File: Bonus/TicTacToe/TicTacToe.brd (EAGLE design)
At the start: 78.4 x 78.4 mm, 61 parts

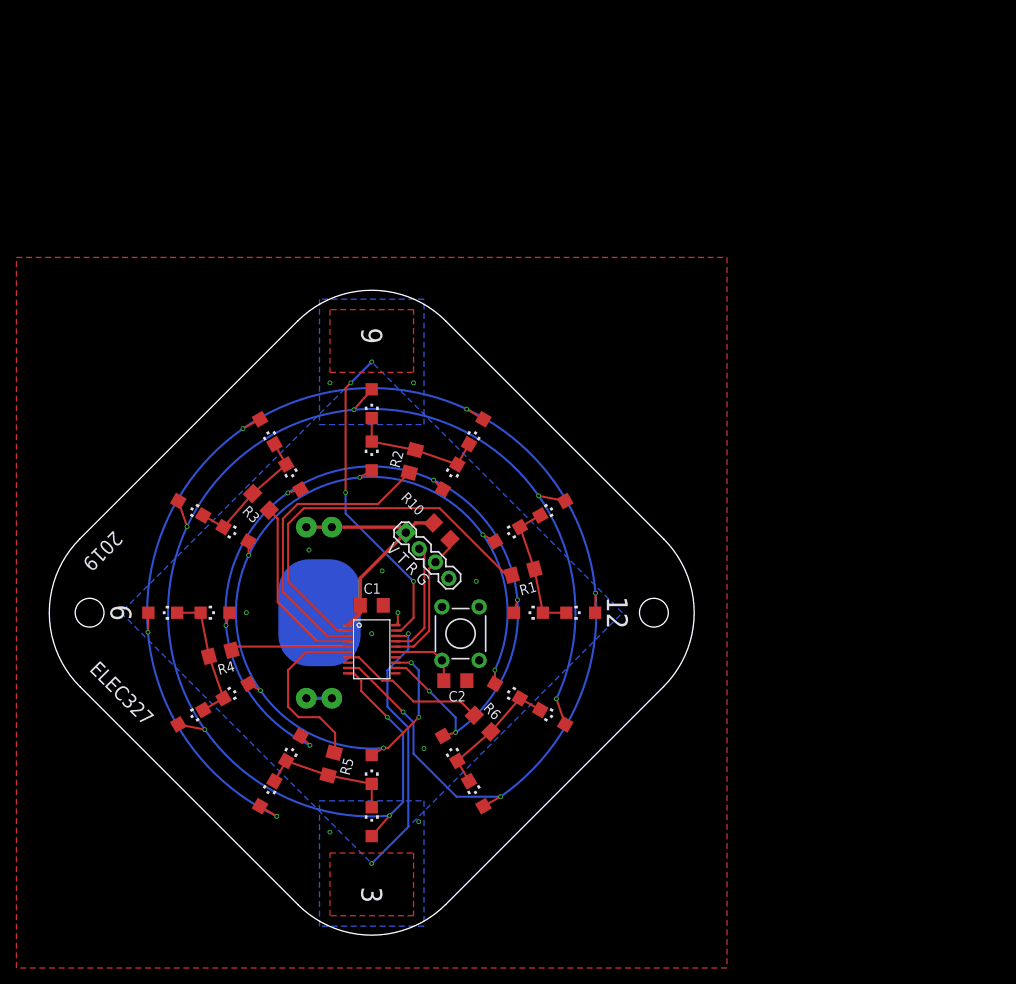
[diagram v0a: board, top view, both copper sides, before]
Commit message: Restored original 2020 pendant in directory, made a new directory for 2021 fabbed pendant, and a directory for Bonus PCB.
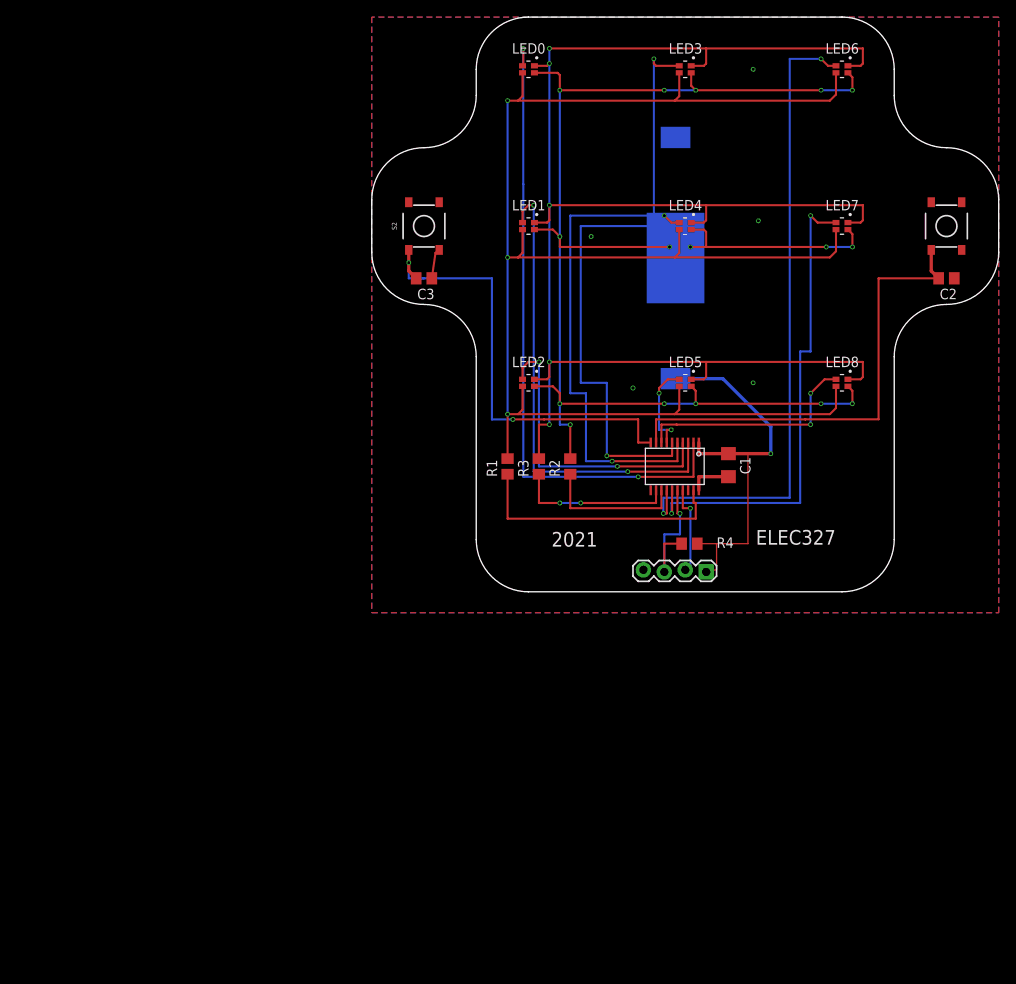
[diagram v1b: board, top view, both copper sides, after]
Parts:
- removed LED10, LED11, LED12, LED13, LED14, LED15, LED16, LED17, LED18, LED19, LED20, LED21, LED22, LED23, LED24, LED9: (no value), led:CHIPLED_1206
- removed LSP1, LSP10, LSP11, LSP12, LSP13, LSP14, LSP15, LSP16, LSP17, LSP18, LSP19, LSP2, LSP20, LSP21, LSP22, LSP23, LSP24, LSP3, LSP4, LSP5, LSP6, LSP7, LSP8, LSP9: LSP10, solpad-mod:LSP10
- removed R10, R5, R6: (no value), rcl:R1206
- added C3: 470nF, rcl:C0805
- added LED0: LTST-C19HE1WT, LTST-C19HE1WT:LED_LTST-C19HE1WT
- added S2: MOMENTARY-SWITCH-SPST-SMD-5.2MM, SparkFun-Switches-Modified:TACTILE_SWITCH_SMD_5.2MM
- BAT1: device Battery:BATTCON_20MM_PTH_COMPACT -> 1060TR:BAT_1060TR
- C2: device rcl:C1206 -> rcl:C0805
- LED1, LED2, LED3, LED4, LED5, LED6, LED7, LED8: value (none) -> LTST-C19HE1WT; device led:CHIPLED_1206 -> LTST-C19HE1WT:LED_LTST-C19HE1WT
- R1, R2, R3, R4: device rcl:R1206 -> rcl:R0805
- S1: value MOMENTARY-SWITCH-SPST-PTH-6.0MM -> MOMENTARY-SWITCH-SPST-SMD-5.2MM; device SparkFun-Switches:TACTILE_SWITCH_PTH_6.0MM -> SparkFun-Switches-Modified:TACTILE_SWITCH_SMD_5.2MM
- moved LED6 98.6 mm to (57.1, 66.0), turned to 270 degrees
- moved LED4 79.0 mm to (38.1, 47.0)
- moved C2 77.2 mm to (69.8, 40.6)
- moved S1 77.1 mm to (69.8, 47.0)
- moved BAT1 74.3 mm to (38.7, 59.1)
- moved LED5 71.2 mm to (38.1, 27.9), turned to 270 degrees
- moved LED3 67.2 mm to (38.1, 66.0), turned to 270 degrees
- moved R4 58.5 mm to (38.6, 8.39), turned to 180 degrees
- moved LED8 57.2 mm to (57.1, 27.9), turned to 270 degrees
- moved LED7 49.1 mm to (57.1, 47.0), turned to 270 degrees
- moved LED1 47.4 mm to (19.1, 47.0), turned to 270 degrees
- moved C1 46.6 mm to (43.4, 17.9), turned to 270 degrees
- moved MSP430 43.0 mm to (36.8, 17.8), turned to 180 degrees
- moved JP1 36.9 mm to (40.6, 5.08), turned to 180 degrees
- moved R3 34.1 mm to (20.3, 17.8), turned to 90 degrees
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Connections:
- removed net CAP1: MSP430.19
- removed net CAP2: MSP430.18
- removed net CB1: LED1.A, LED2.A, LED3.A, LED4.A, LED5.A, LED6.A, LSP1.MP, LSP2.MP, LSP3.MP, LSP4.MP, LSP5.MP, LSP6.MP, MSP430.9
- removed net CB2: LED10.A, LED11.A, LED12.A, LED7.A, LED8.A, LED9.A, LSP10.MP, LSP11.MP, LSP12.MP, LSP7.MP, LSP8.MP, LSP9.MP, MSP430.10
- removed net CB3: LED13.A, LED14.A, LED15.A, LED16.A, LED17.A, LED18.A, LSP13.MP, LSP14.MP, LSP15.MP, LSP16.MP, LSP17.MP, LSP18.MP, MSP430.12
- removed net CB4: LED19.A, LED20.A, LED21.A, LED22.A, LED23.A, LED24.A, LSP19.MP, LSP20.MP, LSP21.MP, LSP22.MP, LSP23.MP, LSP24.MP, MSP430.13
- removed net N$3: MSP430.2, R1.1
- removed net N$4: MSP430.3, R2.1
- removed net N$5: MSP430.4, R3.1
- removed net N$6: MSP430.5, R4.1
- removed net N$7: MSP430.6, R5.1
- removed net N$8: MSP430.7, R6.1
- removed net N$9: MSP430.14
- removed net SWITCH1: C2.2, MSP430.15, S1.1
- new net BLUE: LED0.3, LED1.3, LED2.3, LED3.3, LED4.3, LED5.3, LED6.3, LED7.3, LED8.3, R1.2
- new net CA0: LED0.4, MSP430.2
- new net CA7: LED7.4, MSP430.15
- new net CA8: LED8.4, MSP430.8
- new net CB0: MSP430.19, R1.1
- new net GREEN: LED0.2, LED1.2, LED2.2, LED3.2, LED4.2, LED5.2, LED6.2, LED7.2, LED8.2, R2.2
- new net N$2: MSP430.13, R2.1
- new net RED: LED0.1, LED1.1, LED2.1, LED3.1, LED4.1, LED5.1, LED6.1, LED7.1, LED8.1, R3.2
- new net SW0: C2.2, MSP430.9, S1.1
- new net SW1: C3.2, MSP430.10, S2.1
- net CA1: now also LED1.4, MSP430.3; no longer LED1.C, LED13.C, LED19.C, LED7.C, R1.2
- net CA2: now also LED2.4, MSP430.4; no longer LED14.C, LED2.C, LED20.C, LED8.C, R2.2
- net CA3: now also LED3.4, MSP430.5; no longer LED15.C, LED21.C, LED3.C, LED9.C, R3.2
- net CA4: now also LED4.4, MSP430.6; no longer LED10.C, LED16.C, LED22.C, LED4.C, R4.2
- net CA5: now also LED5.4, MSP430.7; no longer LED11.C, LED17.C, LED23.C, LED5.C, R5.2
- net CA6: now also LED6.4, MSP430.14; no longer LED12.C, LED18.C, LED24.C, LED6.C, R6.2
- net GND: now also BAT1.-, C3.1, S2.3; no longer BAT1.2
- net N$1: now also MSP430.12, R3.1; no longer MSP430.8
- net VDD: now also BAT1.+, R4.1; no longer BAT1.1, BAT1.3, BAT1.4, BAT1.5, R10.1
- net _RST: now also R4.2; no longer R10.2
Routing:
- net RED: track 0.00 -> 197.5 mm, vias 0 -> 5
- net BLUE: track 0.00 -> 193.7 mm, vias 0 -> 3
- net GREEN: track 0.00 -> 182.6 mm, vias 0 -> 16
- net CB1: track 178.1 -> 0.00 mm, vias 1 -> 0
- net CB2: track 164.7 -> 0.00 mm, vias 1 -> 0
- net CB3: track 110.1 -> 0.00 mm, vias 1 -> 0
- net CB4: track 107.3 -> 0.00 mm, vias 2 -> 0
- net CA0: track 0.00 -> 79.1 mm, vias 0 -> 2
- net CA6: track 16.5 -> 79.8 mm, vias 0 -> 2
- net CA3: track 16.5 -> 78.1 mm, vias 0 -> 2
- net CA7: track 0.00 -> 59.4 mm, vias 0 -> 2
- net SW0: track 0.00 -> 58.1 mm
- net SW1: track 0.00 -> 55.5 mm, vias 0 -> 2
- net N$3: track 48.1 -> 0.00 mm
- net CA1: track 16.5 -> 57.7 mm, vias 0 -> 2
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- removed copper zone on layer 1, net CAP1
- removed copper zone on layer 1, net CAP2
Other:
- board size 78.4 x 78.4 mm -> 76.2 x 69.8 mm
- board text added: "2021"
- board text removed: "12"
- board text removed: "2019"
- board text removed: "3"
- board text removed: "6"
- board text removed: "9"
- board text removed: "V T R G"
